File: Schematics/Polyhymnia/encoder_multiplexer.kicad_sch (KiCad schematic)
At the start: 28 parts, among them J7 Serial-Out, Q10 BC547, Q11 BC547, Q12 BC547, Q13 BC547, Q14 BC547, Q15 BC547, Q16 BC547, Q5 BC547, Q6 BC547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

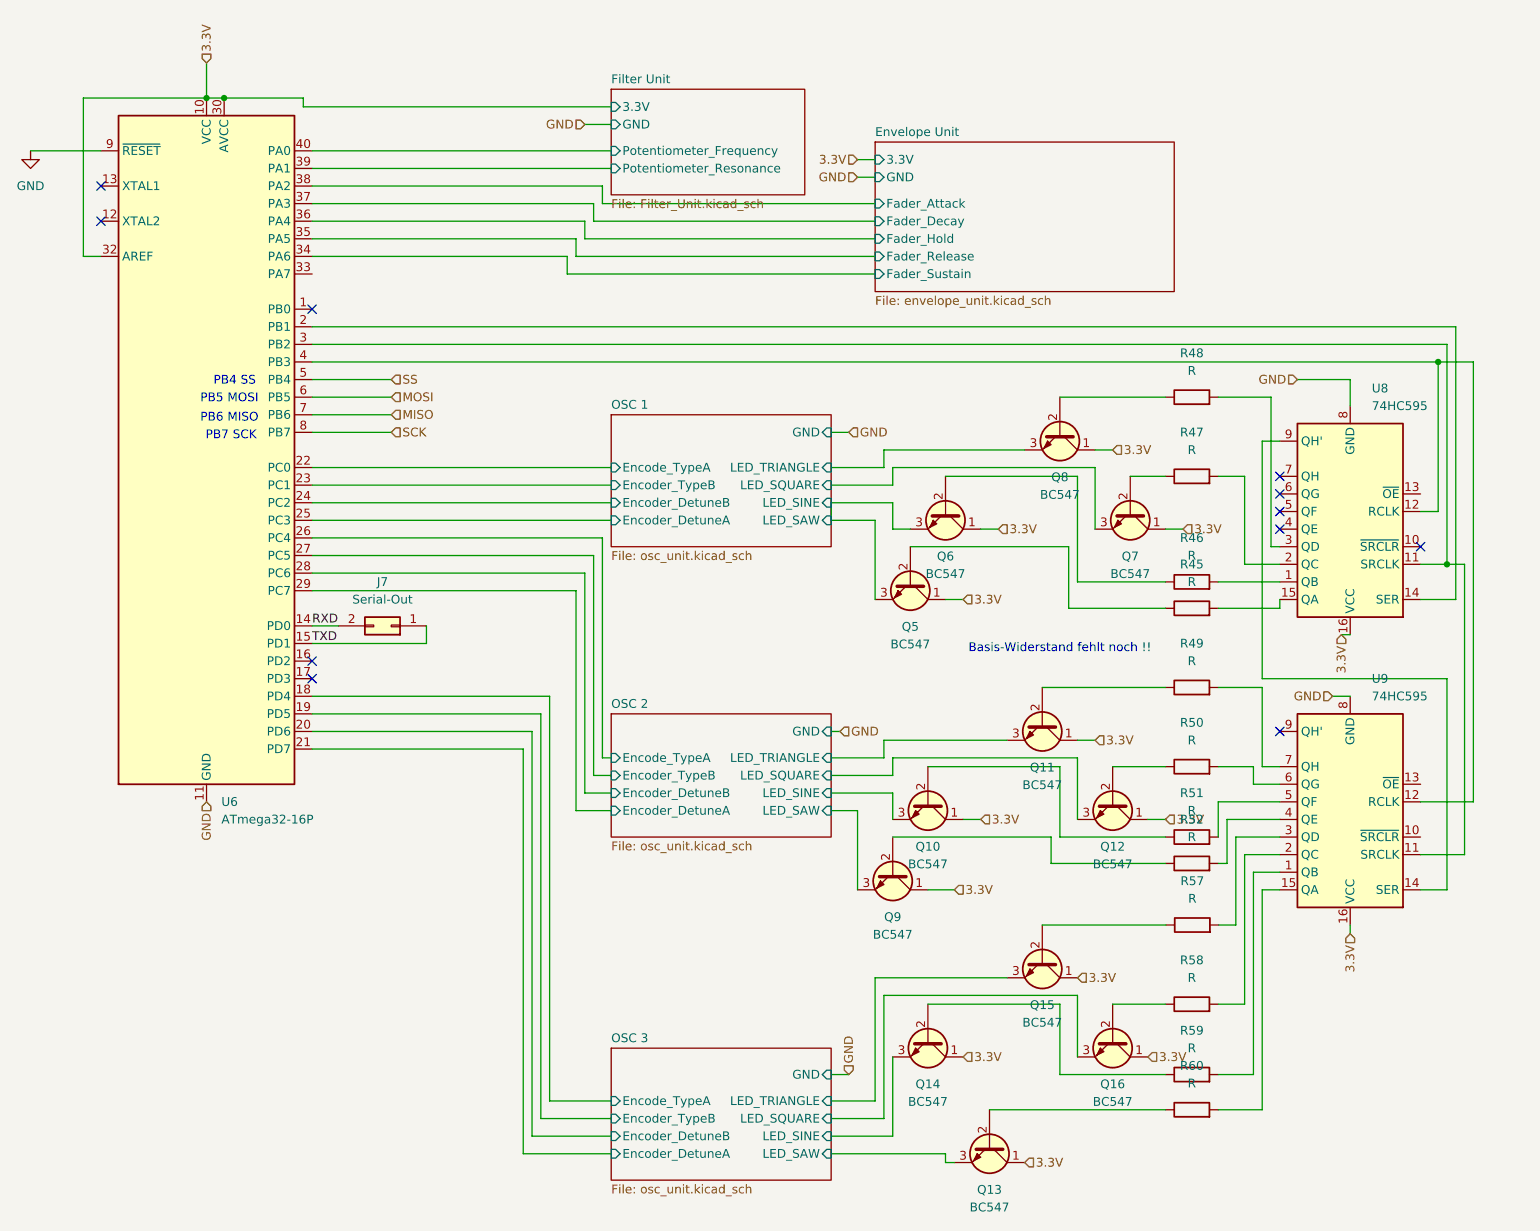
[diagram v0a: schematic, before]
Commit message: Added audio amplifier schematics
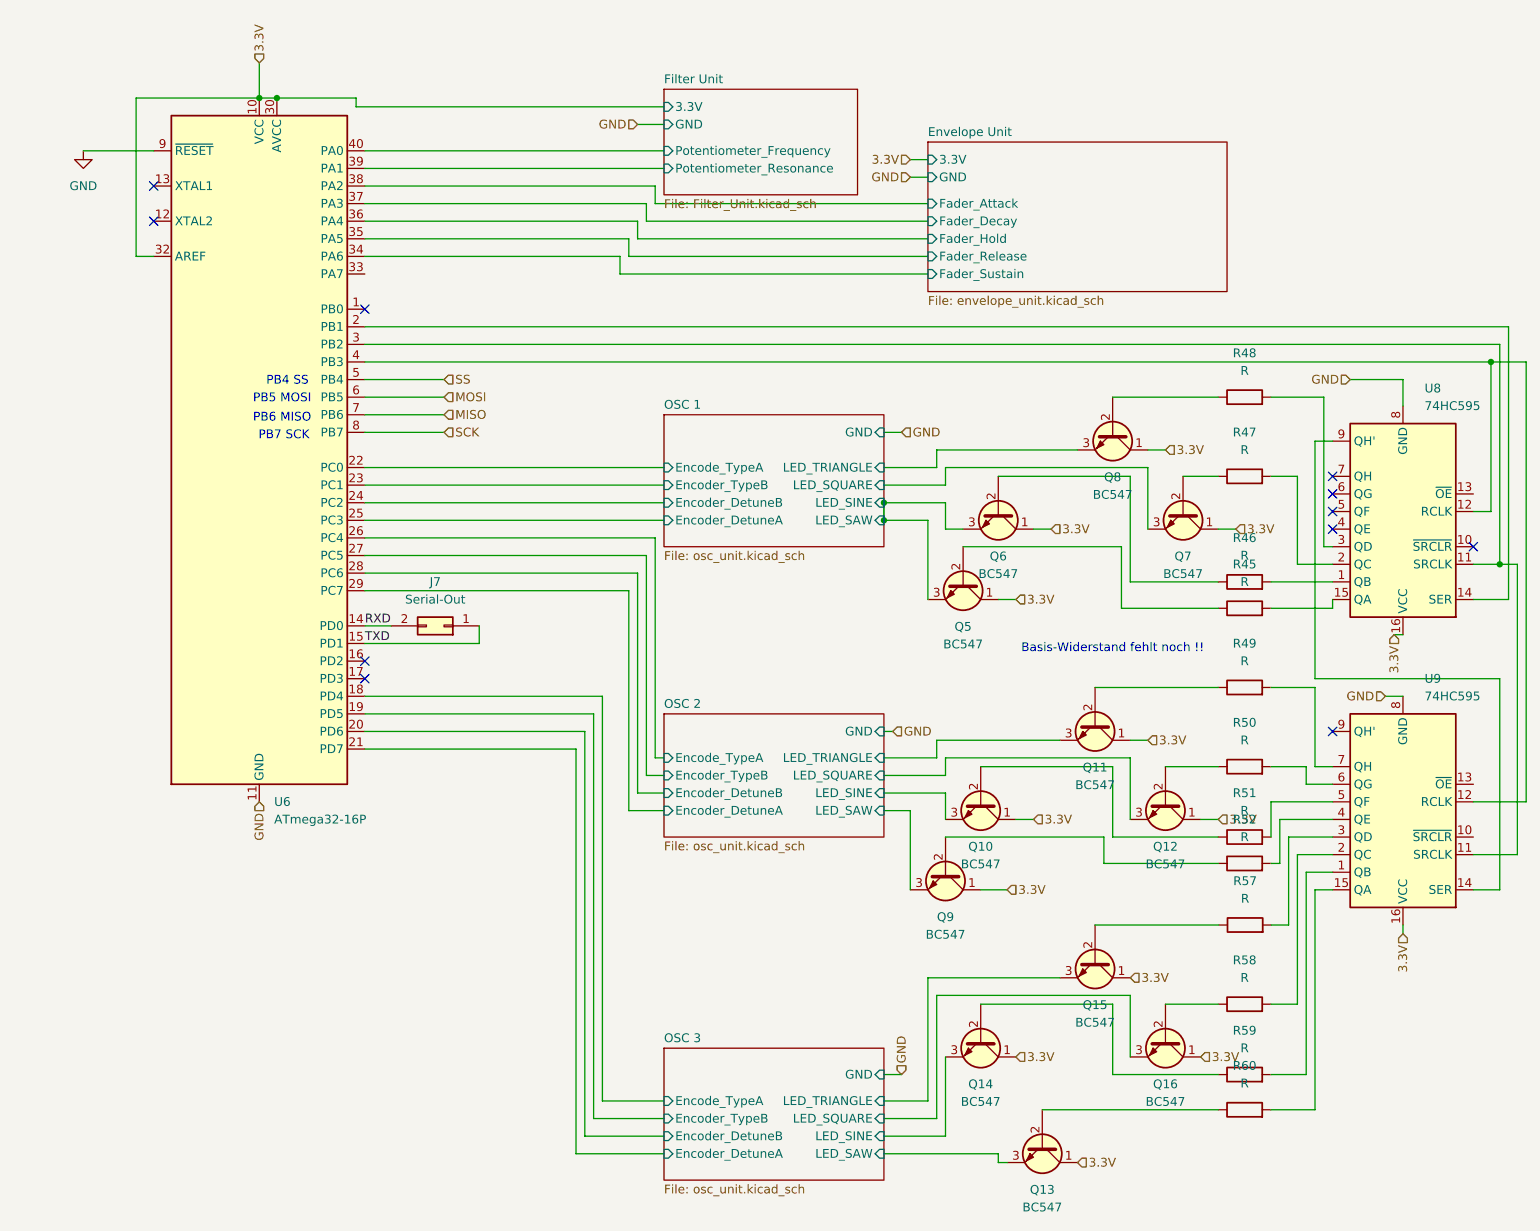
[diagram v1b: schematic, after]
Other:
- title: (none) -> Encoder Control Unit
- moved on the sheet: J7, Q10, Q11, Q12, Q13, Q14, Q15, Q16, Q5, Q6, Q7, Q8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
